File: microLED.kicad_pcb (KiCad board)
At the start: 2 copper layers, 25 x 15 mm, 9 parts, among them J1 IN, J2 OUT

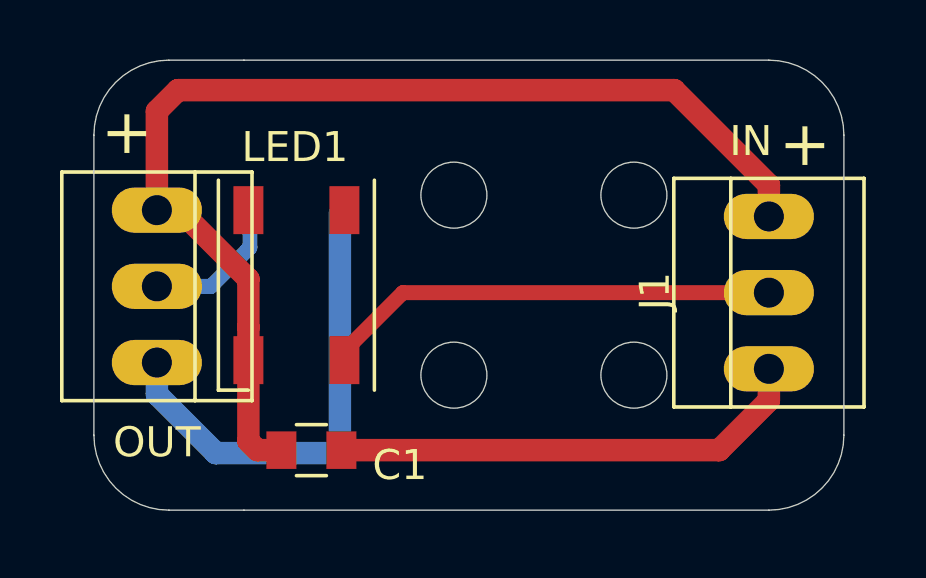
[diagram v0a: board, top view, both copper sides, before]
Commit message: fixed gnd pad not connected on output side
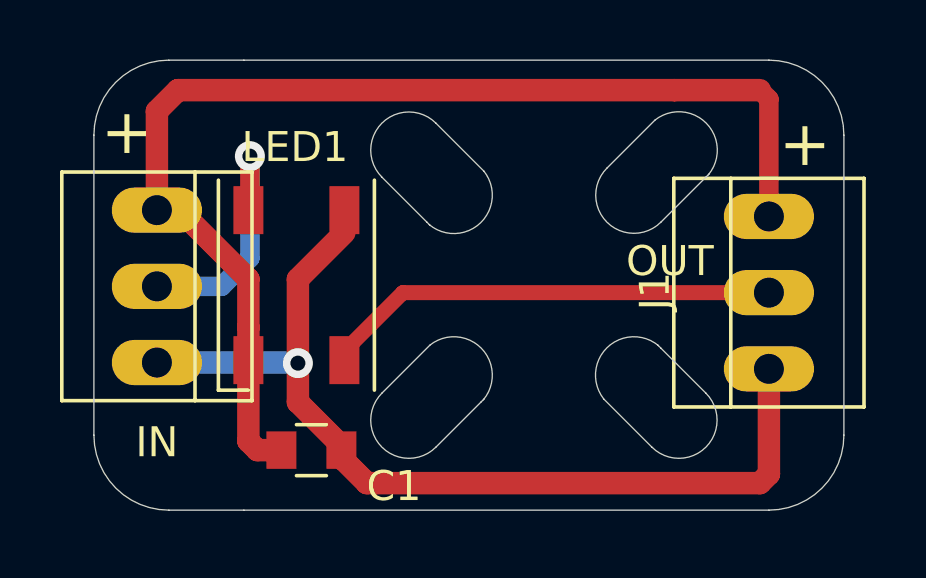
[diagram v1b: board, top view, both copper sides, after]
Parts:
- removed REF** (x4): MountingHole_2.2mm_M2, Mounting_Holes:MountingHole_2.2mm_M2
- J1: value IN -> OUT
- J2: value OUT -> IN
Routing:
- net Net-(J2-Pad2): track 4.78 -> 8.71 mm, vias 0 -> 1
- net Net-(C1-Pad2): track 37.0 -> 38.7 mm
- net Net-(C1-Pad1): track 32.0 -> 32.8 mm, vias 0 -> 1
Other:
- outline, holes or cut-outs redrawn
- net class newTrack added: clearance 0.2, trace_width 0.5, via_dia 0.6, via_drill 0.4
- board text added: "WS2812B"
- board text removed: "8.5mm motor WS2812B"
